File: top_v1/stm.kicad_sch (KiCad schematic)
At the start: 5 parts, among them J10 Conn_02x17_Odd_Even, J2 Conn_01x02_Pin, J7 Conn_02x16_Odd_Even, J8 Conn_02x16_Odd_Even, J9 Conn_02x30_Odd_Even

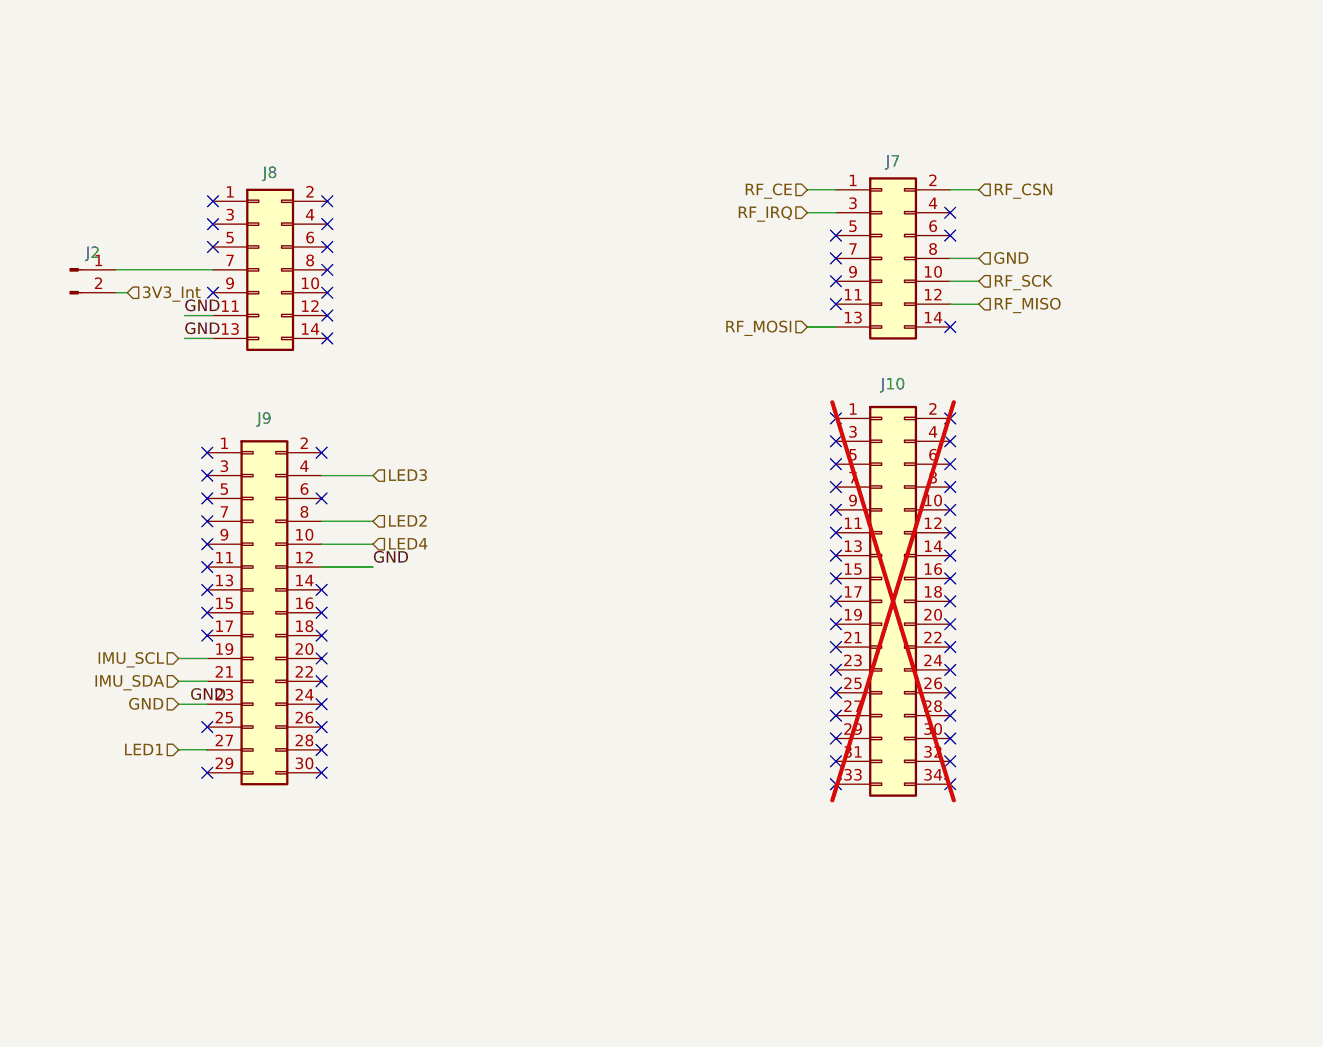
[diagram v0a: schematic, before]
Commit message: File structure enhanced.
Added uniform titleblocks and 3D renders for easier view, file cleanups.
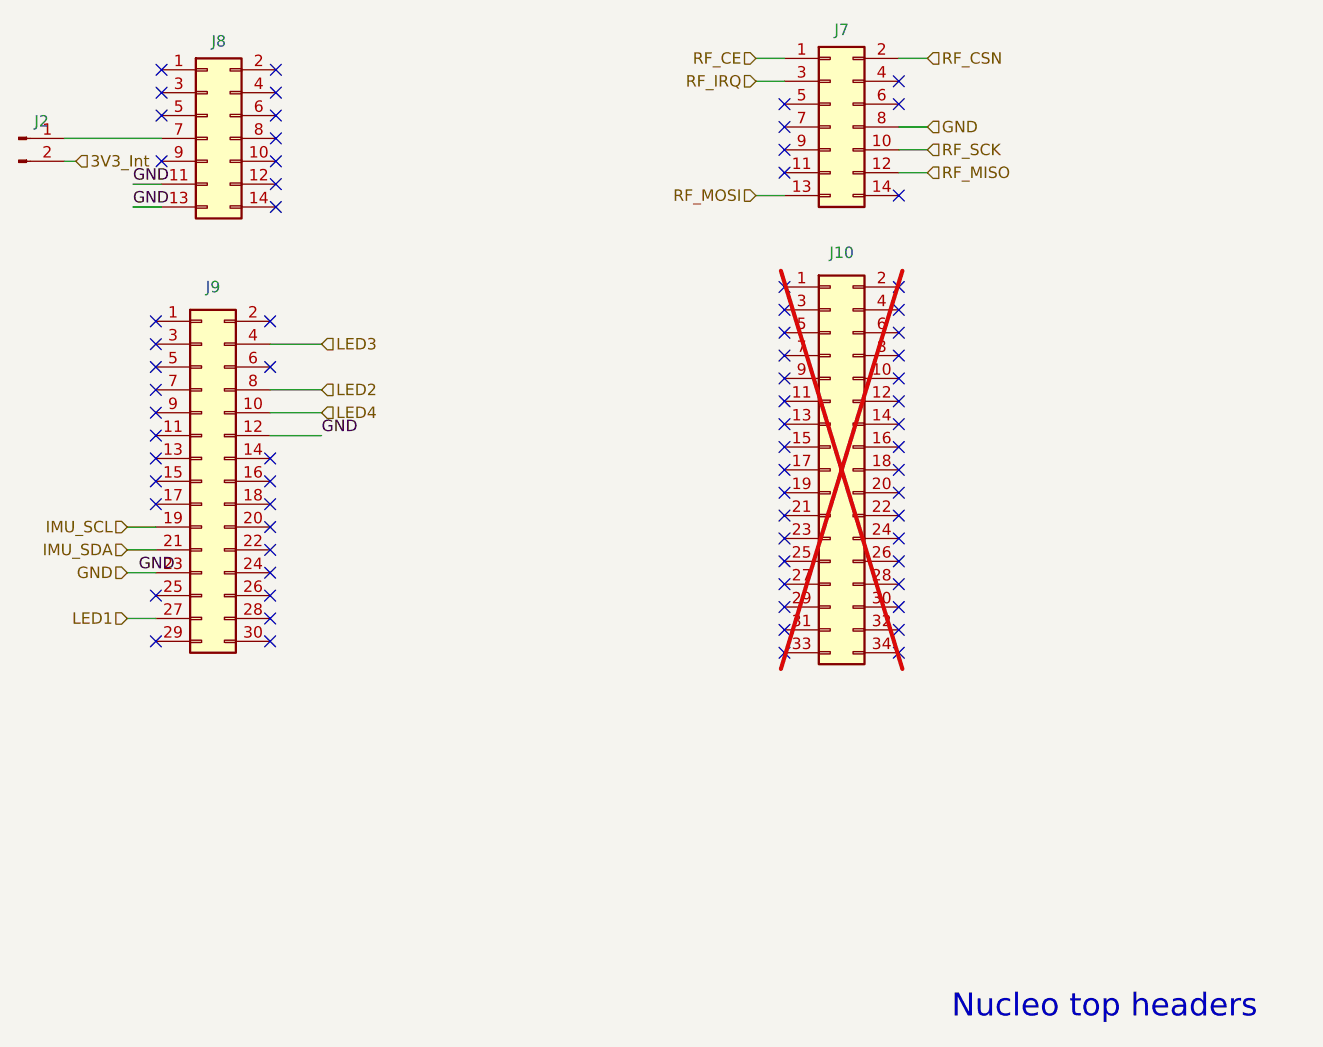
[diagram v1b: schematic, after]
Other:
- note added: "Nucleo top headers"
- title: (none) -> Top board - nRF and IMU to Nucleo H755ZI
- moved on the sheet: J10, J2, J7, J8, J9
